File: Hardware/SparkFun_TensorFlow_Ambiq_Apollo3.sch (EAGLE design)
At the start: 89 parts, among them J5 CORTEX_DEBUG_PTH, J6 CAMERA-0V7670, M1 MEMS_MICROPHONESPW2430HR5H-B, M2 MEMS_MICROPHONESPW2430HR5H-B, U1 AMBIQ-APOLLO3KBR, U2 LIS2DH12, U3 1.8V, U4 LMV358, Y1 32MHz, Y2 32.768kHz

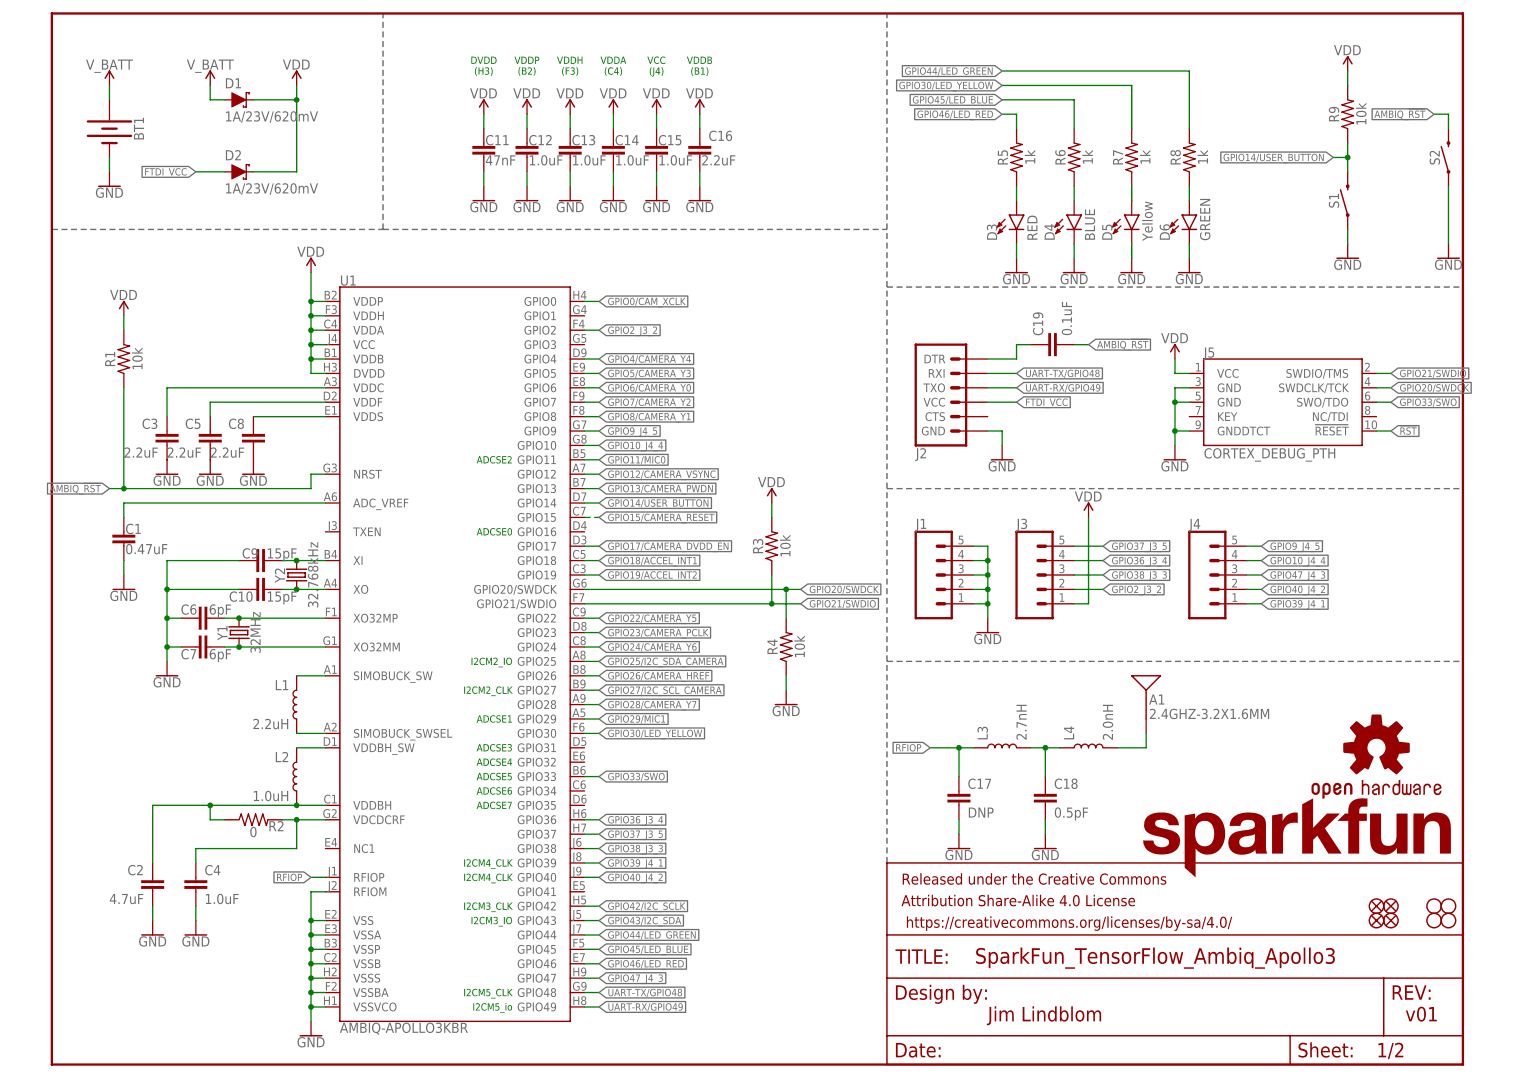
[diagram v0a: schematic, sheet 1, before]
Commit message: Setting trace width/clearance to 5mil, via size to .2mm min
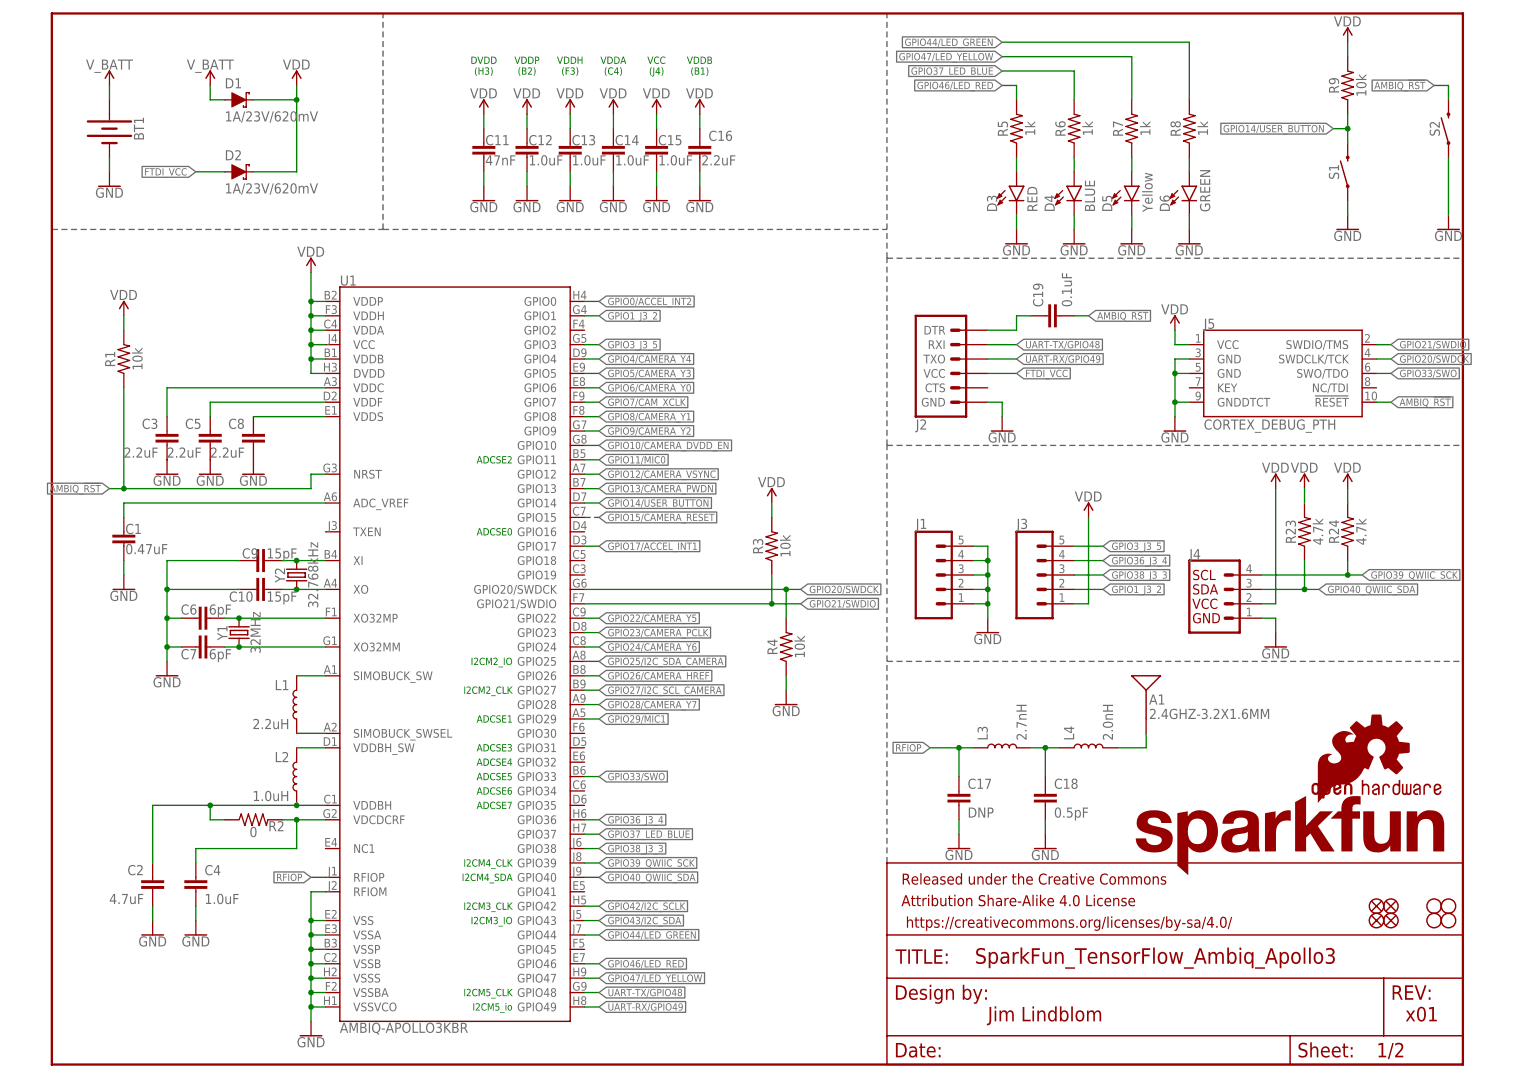
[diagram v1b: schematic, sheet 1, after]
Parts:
- added R23, R24: 4.7k, SparkFun-Resistors:4.7KOHM-0603-1/10W-1%
- added R25, R26: 10k, ambiq:10KOHM-0402-TIGHT-1/10W-1%
- J4: device SparkFun-Connectors:CONN_05NO_SILK -> SparkFun-Connectors:QWIIC_CONNECTORJS-1MM
- LOGO1: value SFE_LOGO_NAME.1_INCH -> SFE_LOGO_NAME_FLAME.1_INCH; device SparkFun-Aesthetics:SFE_LOGO_NAME.1_INCH -> SparkFun-Aesthetics:SFE_LOGO_NAME_FLAME.1_INCH
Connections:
- removed net !RST: J5.!RESET
- removed net GPIO0/CAM_XCLK: J6.XCLK1, U1.GPIO0
- removed net GPIO10_J4_4: J4.4, U1.GPIO10
- removed net GPIO17/CAMERA_DVDD_EN: R11.2, U1.GPIO17, U3.EN
- removed net GPIO18/ACCEL_INT1: U1.GPIO18, U2.INT1
- removed net GPIO19/ACCEL_INT2: U1.GPIO19, U2.INT2
- removed net GPIO2_J3_2: J3.2, U1.GPIO2
- removed net GPIO30/LED_YELLOW: R7.2, U1.GPIO30
- removed net GPIO37_J3_5: J3.5, U1.GPIO37
- removed net GPIO39_J4_1: J4.1, U1.GPIO39
- removed net GPIO40_J4_2: J4.2, U1.GPIO40
- removed net GPIO45/LED_BLUE: R6.2, U1.GPIO45
- removed net GPIO47_J4_3: J4.3, U1.GPIO47
- removed net GPIO7/CAMERA_Y2: J6.Y2, U1.GPIO7
- removed net GPIO9_J4_5: J4.5, U1.GPIO9
- new net GPIO0/ACCEL_INT2: R25.2, U1.GPIO0, U2.INT2
- new net GPIO10/CAMERA_DVDD_EN: R11.2, U1.GPIO10, U3.EN
- new net GPIO17/ACCEL_INT1: R26.2, U1.GPIO17, U2.INT1
- new net GPIO1_J3_2: J3.2, U1.GPIO1
- new net GPIO37_LED_BLUE: R6.2, U1.GPIO37
- new net GPIO39_QWIIC_SCK: J4.4, R24.1, U1.GPIO39
- new net GPIO3_J3_5: J3.5, U1.GPIO3
- new net GPIO40_QWIIC_SDA: J4.3, R23.1, U1.GPIO40
- new net GPIO47/LED_YELLOW: R7.2, U1.GPIO47
- new net GPIO7/CAM_XCLK: J6.XCLK1, U1.GPIO7
- new net GPIO9/CAMERA_Y2: J6.Y2, U1.GPIO9
- net AMBIQ_!RST: now also J5.!RESET
- net GND: now also J4.1
- net VDD: now also J4.2, R23.2, R24.2, R25.1, R26.1
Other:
- note added: "I2CM4_SDA"
- note added: "x01"
- note removed: "v01"
- moved on the sheet: C19, D3, D4, D5, D6, J2, J5, R5, R6, R7, R8, R9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

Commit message: Checklist cleanup of schematic.
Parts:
- FRAME2: VERSION (none) -> x01
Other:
- note added: "Ambiq Apollo3"
- note added: "Ambiq Decoupling"
- note added: "Apollo3 Supply Range: 1.755-3.63V"
- note added: "BLE Antenna"
- note added: "Coin Cell/FTDI Power"
- note added: "Expansion Headers"
- note added: "I2C Address: 0x19 (SA0 = 1)"
- note added: "I2C Address: 0x21"
- note added: "MEMS Microphone - Knowles PW2430HR5H-B"
- note added: "OV7670 VGA Camera"
- note added: "Programming Headers"
- note added: "UI - LEDs and Button"
- note removed: "recommended voltage on dvdd is 1.8. absolute max is 3V. Chance it?"
- moved on the sheet: C19, D3, D4, D5, D6, R5, R6, R7, R8, R9, S1, S2

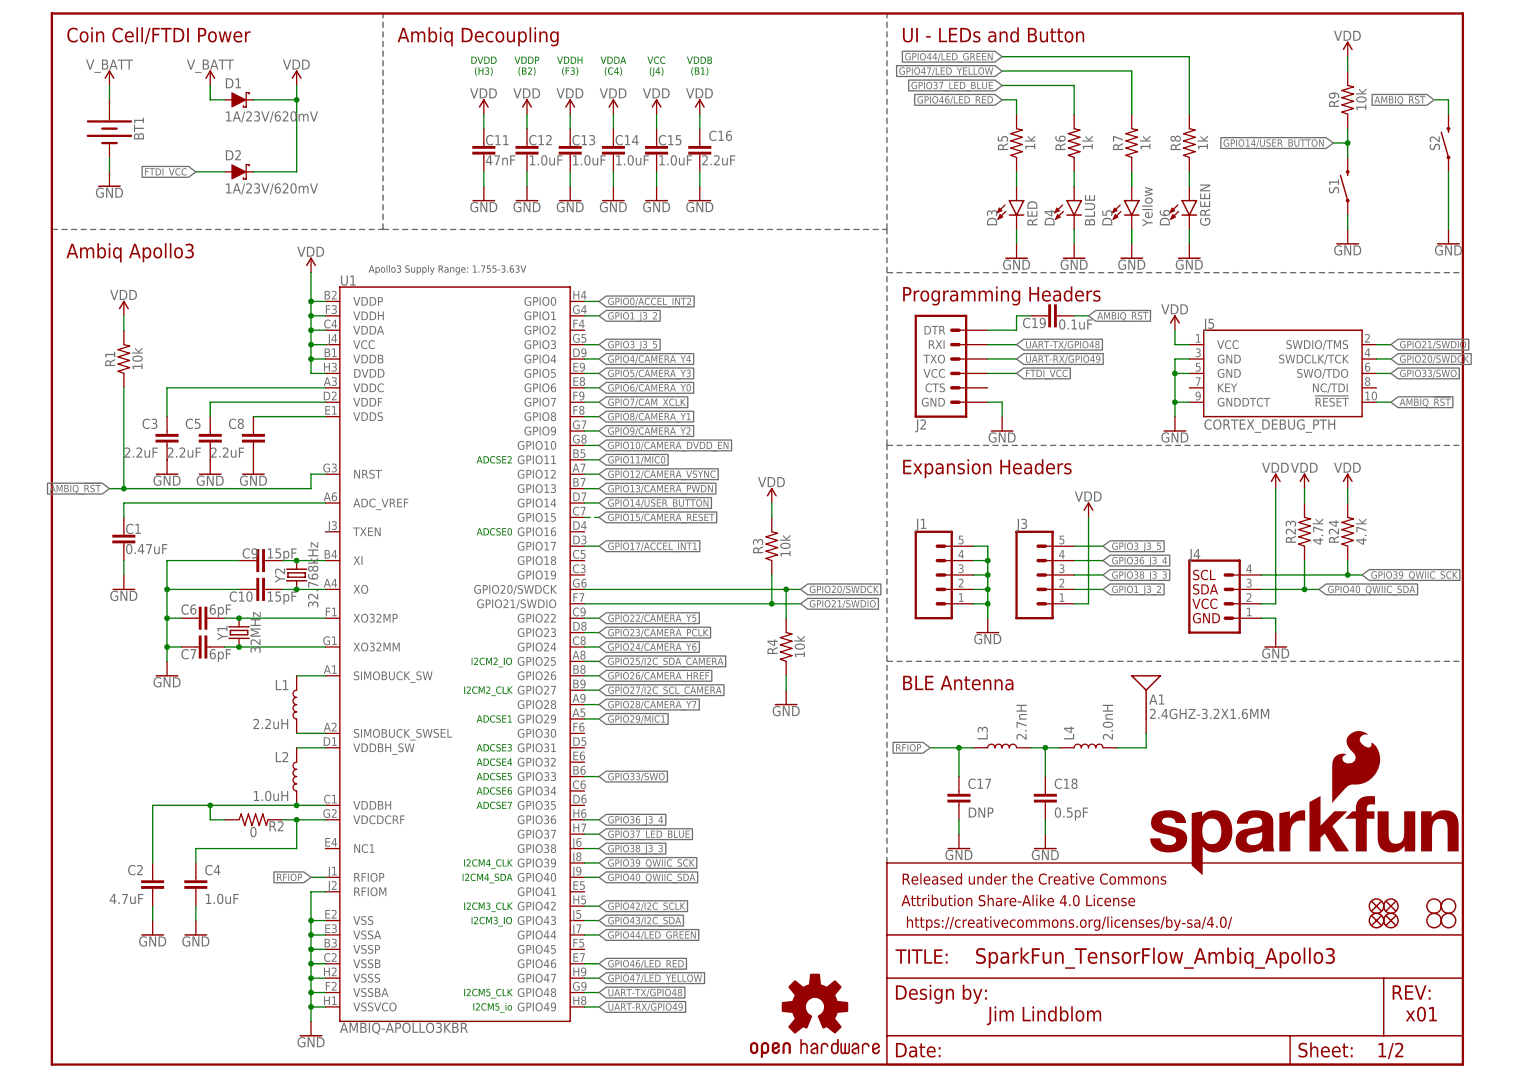
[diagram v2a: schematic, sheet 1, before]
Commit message: Adding v01 of Tensorflow
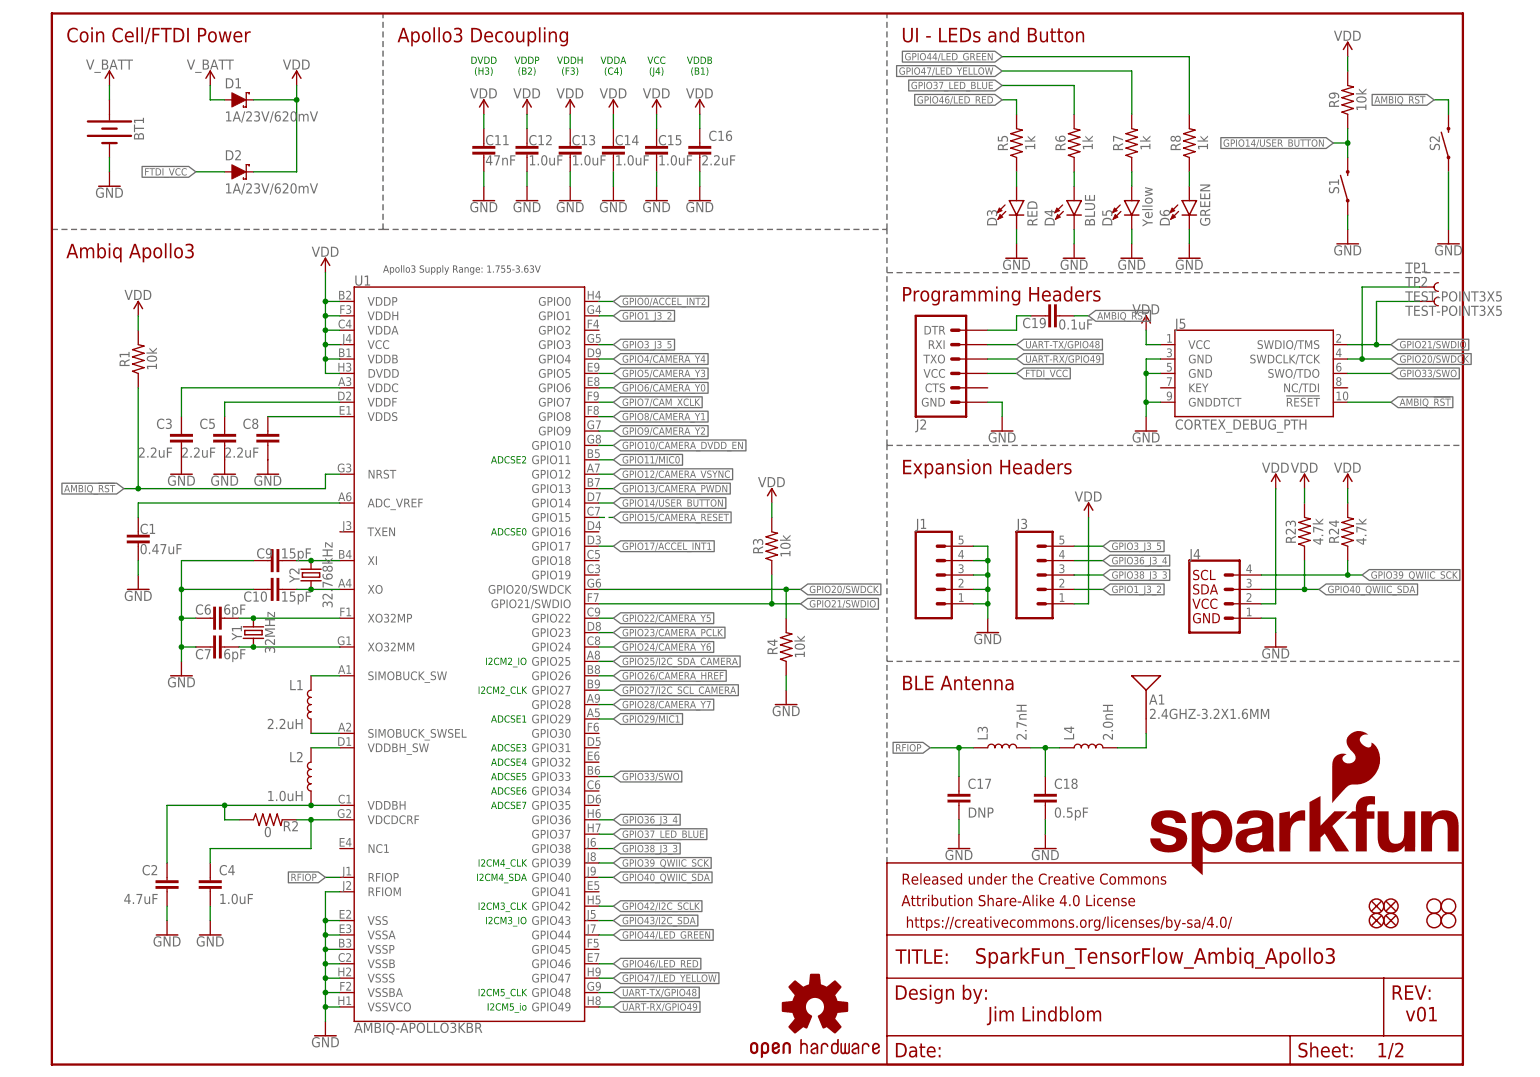
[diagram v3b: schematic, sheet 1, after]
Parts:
- added TP1, TP2: TEST-POINT3X5, SparkFun-Connectors:TEST-POINT3X5
- M1, M2: value MEMS_MICROPHONESPW2430HR5H-B -> MEMS_MIC
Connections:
- net GPIO20/SWDCK: now also TP1.1
- net GPIO21/SWDIO: now also TP2.1
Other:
- note added: "Apollo3 Decoupling"
- note added: "v01"
- note removed: "Ambiq Decoupling"
- note removed: "x01"
- moved on the sheet: C1, C10, C2, C3, C4, C5, C6, C7, C8, C9, J5, L1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

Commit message: Disconnecting DVDD from VDD, adding test points.
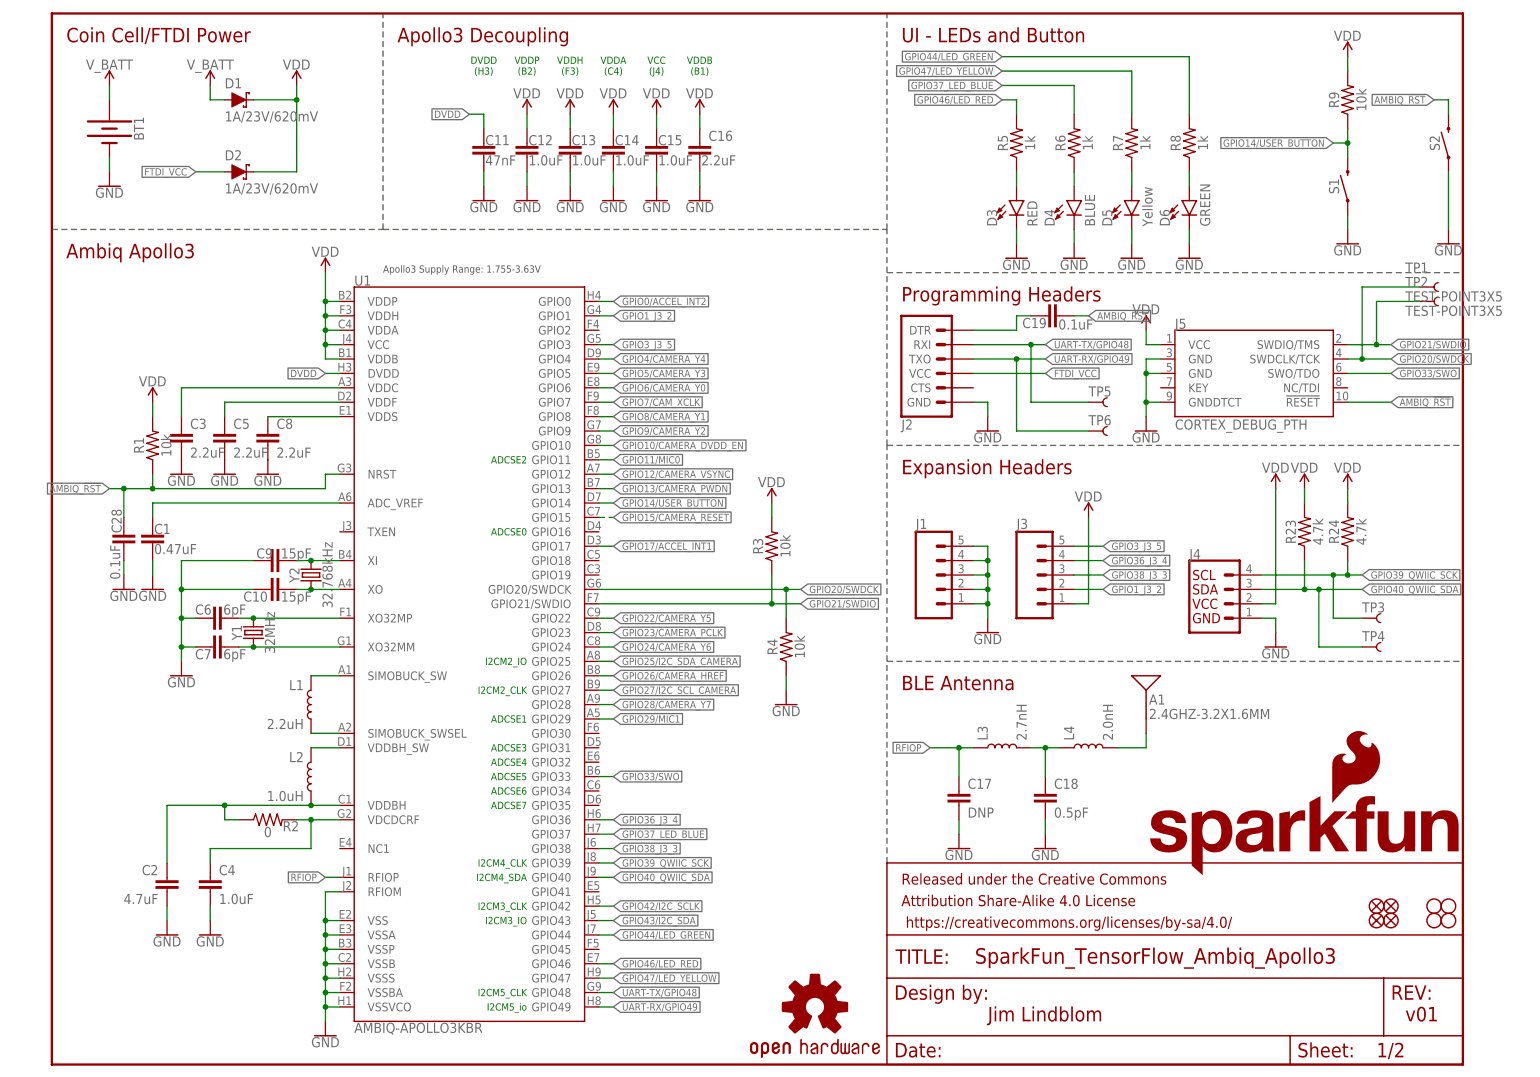
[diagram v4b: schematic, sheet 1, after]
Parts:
- added C28: 0.1uF, ambiq:0.1UF-0402-TIGHT-16V-10%
- added TP3, TP4, TP5, TP6, TP7: TEST-POINT3X5, SparkFun-Connectors:TEST-POINT3X5
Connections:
- new net DVDD: C11.1, U1.DVDD
- net 1.8V: now also TP7.1
- net AMBIQ_!RST: now also C28.1
- net GND: now also C28.2
- net GPIO39_QWIIC_SCK: now also TP3.1
- net GPIO40_QWIIC_SDA: now also TP4.1
- net UART-RX/GPIO49: now also TP6.1
- net UART-TX/GPIO48: now also TP5.1
- net VDD: no longer C11.1, U1.DVDD
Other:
- moved on the sheet: C1, J2, R1
